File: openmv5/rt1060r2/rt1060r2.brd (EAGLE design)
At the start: 35.6 x 44.5 mm, 250 parts, among them CN1 S2B-PH-K-S(LF)(SN), IC1 LM66200DRLR, IC2 TCR2LF33,LM_CT, IC3 AP61300Z6-7, IC4 IS42S16160G-6BL, IC5 IS25LP128F-JKLE-TR, IC6 ATECC608B-MAHDA-T, IC7 MXC4005XC, IC8 KSZ8081RNDCA-TR, IC9 MIMXRT106FCVL5B, J1 USB4105-GF-A, J2 USD-1040310811, J3 DF12-36-DS, J4 DNP, J5 DNP, J6 DNP, J7 DNP, J8 3221-10-0300-00, J9 DNP, M1 9774030151R, M2 9774030151R, Q1 DMG2301L-7, Q2 2N7002KW_R1_00001, Q3 2N7002KW_R1_00001, Q4 2N7002KW_R1_00001, Q5 2N7002KW_R1_00001, U1 BQ24075RGTR, U2 LBEE5KL1DX-883, Y1 ECS-327MVATX-3-CN-TR3, Y2 XRCGB24M000F3M00R0, Y3 SC32S-7PF20PPM

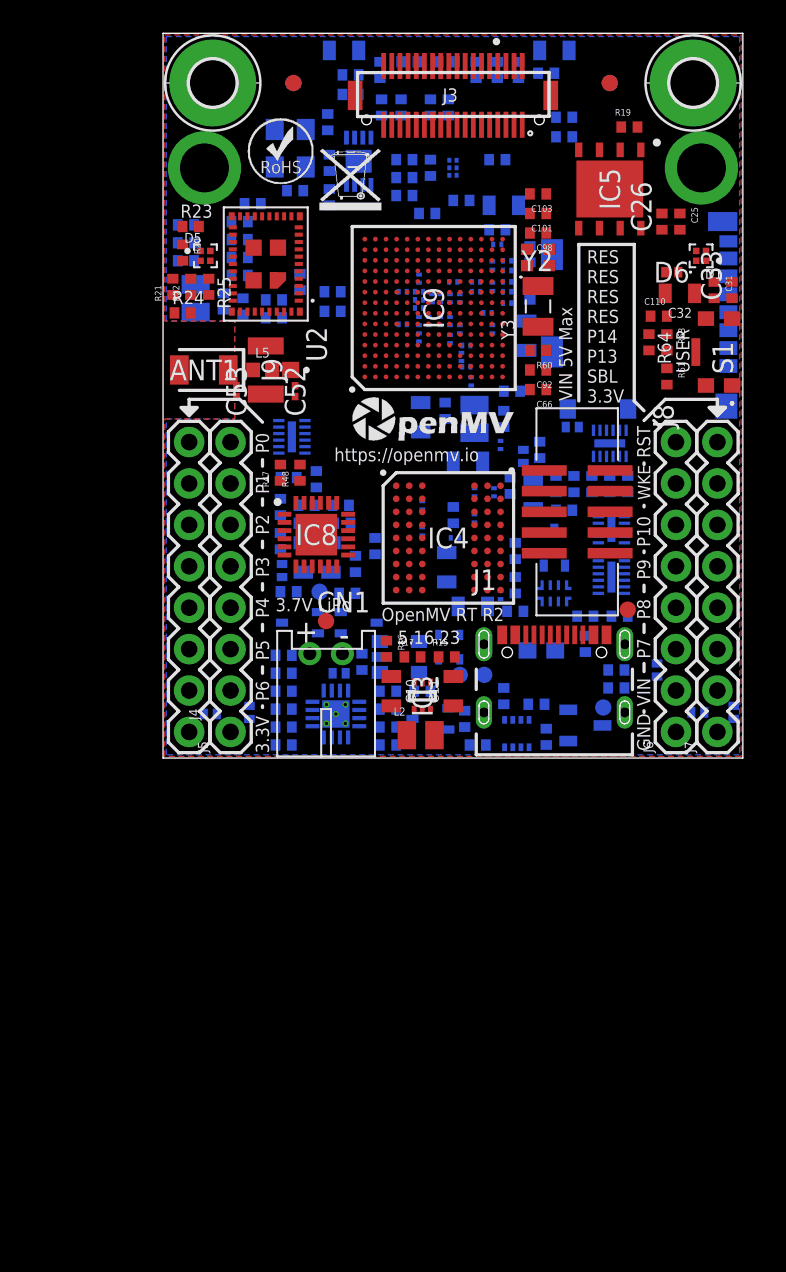
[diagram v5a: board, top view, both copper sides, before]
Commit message: Make the last two I/O pins more configurable
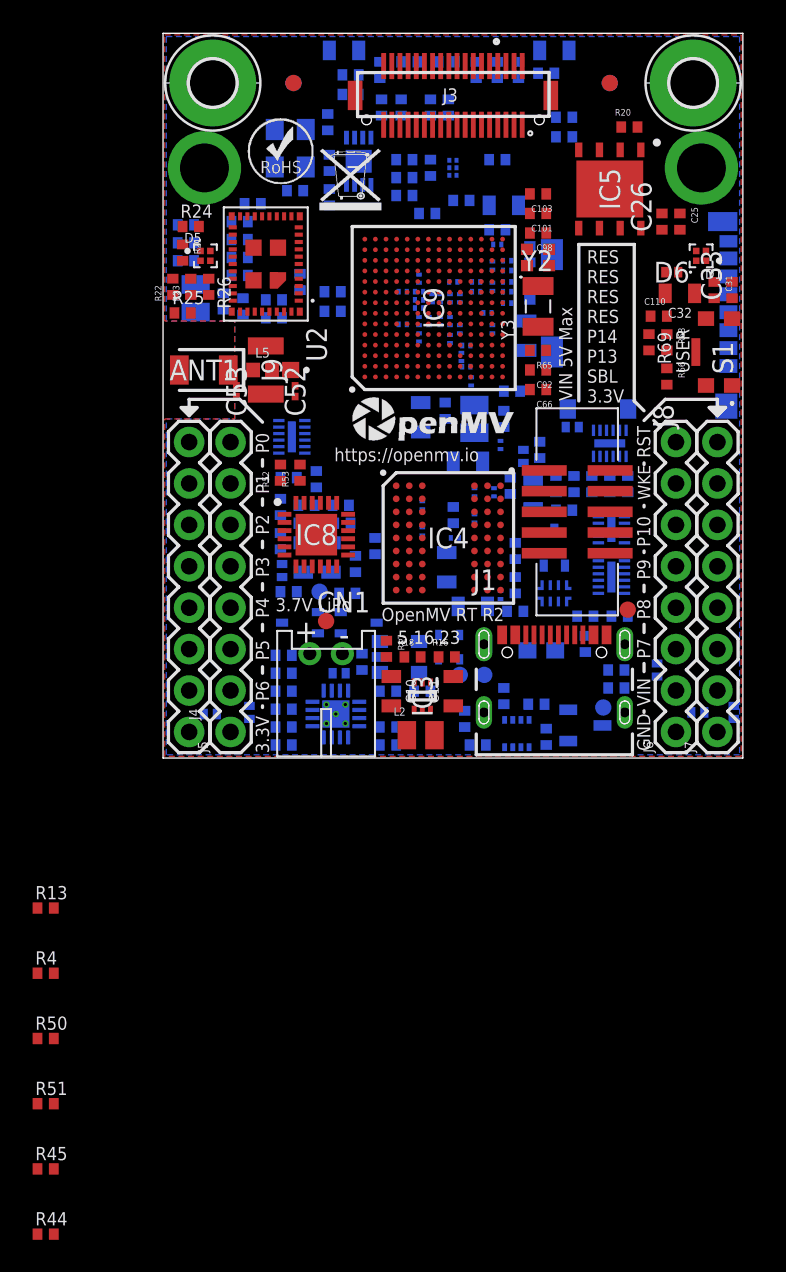
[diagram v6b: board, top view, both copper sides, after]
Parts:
- removed Q5: 2N7002KW_R1_00001, 2N7002KW_R1_00001:SOT65P210X110-3N
- added R65, R69: 100K, 0402:0402
- added R66, R68: 10K, 0402:0402
- added R67: 2.2M, 0402:0402
- R10: value 8.2K -> 46.4K
- R11: value 100K -> 8.2K
- R15: value 200K -> 100K
- R16: value 100K -> 200K
- R17: value 44.2K -> 100K
- R18: value 100K -> 44.2K
- R20, R4, R41: value 1K -> 100K
- R21, R43: value 10K -> 1K
- R22: value 5.1K -> 10K
- R23, R6: value 10K -> 5.1K
- R26: value 2.7K -> 10K
- R29: value 100K -> 2.7K
- R36, R52, R61, R63: value 10K -> 100K
- R38: value 4.7K -> 10K
- R40: value 100K -> 4.7K
- R44: value 10K -> 0
- R45: value DNP -> 0
- R46: value DNP -> 10K
- R47, R57, R58: value 100K -> 10K
- R48: value 220 -> DNP
- R49, R51: value 1K -> DNP
- R5: value 5.1K -> 1K
- R50: value 6.49K -> DNP
- R53: value 10K -> 220
- R54, R56: value 100K -> 1K
- R55: value 100K -> 6.49K
- R59: value 30K -> 100K
- R62: value 2.2M -> 100K
- R64: value 100K -> 30K
- R8: value 1.1K -> 10K
- R9: value 46.4K -> 1.1K
- moved R44 65.8 mm to (-7.20, -29.2), flipped to the top, turned to 0 degrees
- moved R45 46.2 mm to (-7.20, -25.2), flipped to the top, turned to 0 degrees
- moved R13 40.1 mm to (-7.20, -9.20), flipped to the top
- moved R51 38.2 mm to (-7.20, -21.2), flipped to the top, turned to 0 degrees
- moved R50 33.0 mm to (-7.20, -17.2), flipped to the top, turned to 0 degrees
- moved R4 30.0 mm to (-7.20, -13.2), flipped to the top
- moved R20 28.5 mm to (28.6, 38.7), turned to 0 degrees
- moved R46 27.4 mm to (16.2, 33.4), turned to 180 degrees
- moved R61 27.2 mm to (4.70, 30.7), flipped to the bottom, turned to 180 degrees
- moved R19 26.9 mm to (21.6, 12.7), flipped to the bottom, turned to 270 degrees
- moved R63 26.8 mm to (5.50, 34.0), flipped to the bottom, turned to 180 degrees
- moved R55 24.7 mm to (11.3, 10.1), turned to 180 degrees
- moved R60 22.9 mm to (1.40, 32.7), flipped to the bottom, turned to 0 degrees
- moved R35 22.8 mm to (28.5, 16.8), turned to 270 degrees
- moved R48 20.4 mm to (25.9, 7.00), flipped to the bottom
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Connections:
- removed net ON_BATTERY: IC9.P2, Q2.2, R12.1
- new net N$1: J6.3, R45.2
- new net N$2: J6.4, R44.2
- net BT_H_WAKE: now also R58.1; no longer R53.1
- net BT_REG_ON: now also R47.1; no longer R44.1
- net CHG: now also R13.1, R51.2, R6.1; no longer R5.1
- net DCDC_PSWITCH: now also R64.1; no longer R59.1
- net DCMI_D7: now also R46.1; no longer R43.1
- net DCMI_FSIN: now also R42.1; no longer R41.1
- net DCMI_PWDN: now also R38.1; no longer R37.1
- net DCMI_RST: now also R37.1; no longer R36.1
- net DCMI_SCL: now also R39.1; no longer R38.1
- net DCMI_SDA: now also R40.1; no longer R39.1
- net DCMI_SSEL: now also R36.1; no longer R35.1
- net EN: now also Q4.3, R17.1; no longer Q5.3, R16.1
- net ETH_INT: now also R54.1; no longer R49.1
- net ETH_LED: now also R53.1; no longer R48.1
- net ETH_MDIO: now also R56.1; no longer R51.1
- net ETH_RST: now also R52.1; no longer R47.1
- net FB: now also R16.1, R18.2; no longer R15.1, R17.2
- net GND: now also R11.2, R18.1, R37.2, R47.2, R55.2, R67.2; no longer R17.1, R36.2, R44.2, R50.2, R62.2, R7.2
- net ILIM: now also R9.1; no longer R8.1
- net INT_I2C_INT: now also R29.1; no longer R28.1
- net INT_I2C_SCL: now also R27.1; no longer R26.1
- net INT_I2C_SDA: now also R28.1; no longer R27.1
- net ISET: now also R11.1; no longer R10.1
- net JTAG_TDI: now also R50.1
- net JTAG_TDI_INT: now also R44.1, R48.1; no longer J6.4, R45.1
- net JTAG_TDI_INT_UNUSED: now also R48.2; no longer R45.2
- net JTAG_TRSTB: now also R51.1
- net JTAG_TRSTB_INT: now also R45.1, R49.1; no longer J6.3, R46.1
- net JTAG_TRSTB_INT_UNUSED: now also R49.2; no longer R46.2
- net LED_B: now also R21.1, R24.1; no longer R20.1, R23.1
- net LED_B_INT: now also R21.2; no longer R20.2
- net LED_CHG: now also R6.2; no longer R5.2
- net LED_G: now also R22.1, R25.1; no longer R21.1, R24.1
- net LED_G_INT: now also R22.2; no longer R21.2
- net LED_PGOOD: now also R7.2; no longer R6.2
- net LED_R: now also R23.1, R26.1; no longer R22.1, R25.1
- net LED_R_INT: now also R23.2; no longer R22.2
- net LED_ST: now also R5.2; no longer R4.2
- net MDI_LED: now also R53.2; no longer R48.2
- net ONOFF: now also Q3.2; no longer Q4.2
- net P10_PWM: now also R43.1; no longer R42.1
- net P11_WAKEUP: now also Q2.3, R14.1; no longer Q3.3, R13.1
- net P12_RST_N: now also R65.2; no longer R60.2
- net PGOOD: now also IC9.P2, R12.1, R7.1; no longer Q2.3, R11.1, R6.1
- net PMIC_ONOFF: now also Q3.3, R15.1; no longer Q4.3, R14.1
- net PMIC_ON_REQ: now also Q4.2; no longer Q5.2
- net PMIC_STBY_REQ: now also R69.1; no longer R64.1
- net PWM_FSIN: now also R41.1, R43.2; no longer R40.1, R41.2
- net P_FLASH_CE: now also R20.2; no longer R19.2
- net RAW: now also R15.2, R17.2; no longer D1.4, R11.2, R13.2, R16.2
- net REXT: now also R55.1; no longer R50.1
- net SBL: now also R46.2; no longer R43.2
- net SDRAM_CS: now also R19.2; no longer R18.2
- net SD_CD: now also R30.1; no longer R29.1
- net SD_CMD: now also R33.1; no longer R32.1
- net SD_DAT0: now also R32.1; no longer R31.1
- net SD_DAT1: now also R31.1; no longer R30.1
- net SD_DAT2: now also R35.1; no longer R34.1
- net SD_DAT3: now also R34.1; no longer R33.1
- net ST: now also R5.1, R50.2
- net SWITCH: now also R66.1, R68.2; no longer R61.1, R63.2
- net SWITCH_OUT: now also R68.1, R69.2; no longer R63.1, R64.2
- net TMR: now also R10.1; no longer R9.1
- net TS: now also R8.1; no longer R7.1
- net VCC: now also D1.4, R13.2, R16.2, R20.1, R36.2, R4.2, R41.2, R60.2, R62.2, R63.2, R64.2, R65.1, R66.2; no longer Q2.1, R15.2, R18.1, R23.2, R37.2, R47.2, R49.2, R51.2, R53.2, R55.2, R60.1
- net VDD_SNVS: now also Q2.1; no longer Q5.1
- net WAKEUP: now also Q2.2; no longer Q3.2
- net WIFI_CMD: now also R63.1; no longer R58.1
- net WIFI_D0: now also R62.1; no longer R57.1
- net WIFI_D1: now also R61.1; no longer R56.1
- net WIFI_D2: now also R60.1; no longer R55.1
- net WIFI_D3: now also R59.1; no longer R54.1
- net WL_H_WAKE: now also R57.1; no longer R52.1
- net XTALI: now also R67.1; no longer R62.1

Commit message: Cleanup
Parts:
- moved R44 53.6 mm to (29.6, 9.80), flipped to the bottom, turned to 270 degrees
- moved R45 49.3 mm to (29.6, 7.60), flipped to the bottom, turned to 270 degrees
- moved R51 45.1 mm to (13.2, 19.0), flipped to the bottom, turned to 90 degrees
- moved R50 42.2 mm to (14.4, 19.0), flipped to the bottom, turned to 90 degrees
- moved R4 40.6 mm to (14.4, 21.2), flipped to the bottom, turned to 90 degrees
- moved R13 36.6 mm to (13.2, 21.2), flipped to the bottom, turned to 90 degrees
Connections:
- net N$1 renamed P13
- net N$2 renamed P14
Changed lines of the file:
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@@
 <attribute name="VALUE" x="18.905" y="40.535" size="0.8128" layer="28" ratio="10" rot="MR270"/>
 </element>
-<element name="R13" library="0402" package="0402" value="100K" x="-7.2" y="-9.2" smashed="yes">
-<attribute name="MPN" value="AC0402FR-07100KL" x="-7.2" y="-9.2" size="1.778" layer="27" display="off"/>
-<attribute name="NAME" x="-7.835" y="-8.665" size="0.8128" layer="25" ratio="10"/>
-<attribute name="VALUE" x="-7.835" y="-10.605" size="0.8128" layer="27" ratio="10"/>
+<element name="R13" library="0402" package="0402" value="100K" x="13.2" y="21.2" smashed="yes" rot="MR90">
+<attribute name="MPN" value="AC0402FR-07100KL" x="13.2" y="21.2" size="1.778" layer="28" rot="MR90" display="off"/>
+<attribute name="NAME" x="13.735" y="20.565" size="0.8128" layer="26" ratio="10" rot="MR90"/>
+<attribute name="VALUE" x="11.795" y="20.565" size="0.8128" layer="28" ratio="10" rot="MR90"/>
 </element>
-<element name="R4" library="0402" package="0402" value="100K" x="-7.2" y="-13.2" smashed="yes">
-<attribute name="MPN" value="AC0402FR-07100KL" x="-7.2" y="-13.2" size="1.778" layer="27" display="off"/>
-<attribute name="NAME" x="-7.835" y="-12.665" size="0.8128" layer="25" ratio="10"/>
-<attribute name="VALUE" x="-7.835" y="-14.605" size="0.8128" layer="27" ratio="10"/>
+<element name="R4" library="0402" package="0402" value="100K" x="14.4" y="21.2" smashed="yes" rot="MR90">
+<attribute name="MPN" value="AC0402FR-07100KL" x="14.4" y="21.2" size="1.778" layer="28" rot="MR90" display="off"/>
+<attribute name="NAME" x="14.935" y="20.565" size="0.8128" layer="26" ratio="10" rot="MR90"/>
+<attribute name="VALUE" x="12.995" y="20.565" size="0.8128" layer="28" ratio="10" rot="MR90"/>
 </element>
-<element name="R50" library="0402" package="0402" value="DNP" x="-7.2" y="-17.2" smashed="yes">
-<attribute name="MPN" value="DNP" x="-7.2" y="-17.2" size="1.778" layer="27" display="off"/>
-<attribute name="NAME" x="-7.835" y="-16.665" size="0.8128" layer="25" ratio="10"/>
-<attribute name="VALUE" x="-7.835" y="-18.605" size="0.8128" layer="27" ratio="10"/>
+<element name="R50" library="0402" package="0402" value="DNP" x="14.4" y="19" smashed="yes" rot="MR90">
+<attribute name="MPN" value="DNP" x="14.4" y="19" size="1.778" layer="28" rot="MR90" display="off"/>
+<attribute name="NAME" x="14.935" y="18.365" size="0.8128" layer="26" ratio="10" rot="MR90"/>
+<attribute name="VALUE" x="12.995" y="18.365" size="0.8128" layer="28" ratio="10" rot="MR90"/>
 </element>
-<element name="R51" library="0402" package="0402" value="DNP" x="-7.2" y="-21.2" smashed="yes">
-<attribute name="MPN" value="DNP" x="-7.2" y="-21.2" size="1.778" layer="27" display="off"/>
-<attribute name="NAME" x="-7.835" y="-20.665" size="0.8128" layer="25" ratio="10"/>
-<attribute name="VALUE" x="-7.835" y="-22.605" size="0.8128" layer="27" ratio="10"/>
+<element name="R51" library="0402" package="0402" value="DNP" x="13.2" y="19" smashed="yes" rot="MR90">
+<attribute name="MPN" value="DNP" x="13.2" y="19" size="1.778" layer="28" rot="MR90" display="off"/>
+<attribute name="NAME" x="13.735" y="18.365" size="0.8128" layer="26" ratio="10" rot="MR90"/>
+<attribute name="VALUE" x="11.795" y="18.365" size="0.8128" layer="28" ratio="10" rot="MR90"/>
 </element>
-<element name="R45" library="0402" package="0402" value="0" x="-7.2" y="-25.2" smashed="yes">
-<attribute name="MPN" value="RC0402JR-070RL" x="-7.2" y="-25.2" size="1.778" layer="27" display="off"/>
-<attribute name="NAME" x="-7.835" y="-24.665" size="0.8128" layer="25" ratio="10"/>
-<attribute name="VALUE" x="-7.835" y="-26.605" size="0.8128" layer="27" ratio="10"/>
+<element name="R45" library="0402" package="0402" value="0" x="29.6" y="7.6" smashed="yes" rot="MR270">
+<attribute name="MPN" value="RC0402JR-070RL" x="29.6" y="7.6" size="1.778" layer="28" rot="MR270" display="off"/>
+<attribute name="NAME" x="29.065" y="8.235" size="0.8128" layer="26" ratio="10" rot="MR270"/>
+<attribute name="VALUE" x="31.005" y="8.235" size="0.8128" layer="28" ratio="10" rot="MR270"/>
 </element>
-<element name="R44" library="0402" package="0402" value="0" x="-7.2" y="-29.2" smashed="yes">
-<attribute name="MPN" value="RC0402JR-070RL" x="-7.2" y="-29.2" size="1.778" layer="27" display="off"/>
-<attribute name="NAME" x="-7.835" y="-28.665" size="0.8128" layer="25" ratio="10"/>
-<attribute name="VALUE" x="-7.835" y="-30.605" size="0.8128" layer="27" ratio="10"/>
+<element name="R44" library="0402" package="0402" value="0" x="29.6" y="9.8" smashed="yes" rot="MR270">
+<attribute name="MPN" value="RC0402JR-070RL" x="29.6" y="9.8" size="1.778" layer="28" rot="MR270" display="off"/>
+<attribute name="NAME" x="29.065" y="10.435" size="0.8128" layer="26" ratio="10" rot="MR270"/>
+<attribute name="VALUE" x="31.005" y="10.435" size="0.8128" layer="28" ratio="10" rot="MR270"/>
 </element>
 </elements>
@@
 <wire x1="17.3" y1="21.8" x2="18.875" y2="23.375" width="0" layer="19" extent="1-16"/>
 <wire x1="15.8" y1="21.8" x2="17.3" y2="21.8" width="0" layer="19" extent="16-16"/>
+<wire x1="14.4" y1="21.7" x2="15.8" y2="21.8" width="0" layer="19" extent="16-16"/>
+<wire x1="13.2" y1="21.7" x2="14.4" y2="21.7" width="0" layer="19" extent="16-16"/>
 <wire x1="21.9" y1="22.5" x2="18.9" y2="23.35" width="0" layer="19" extent="16-16"/>
 <wire x1="22.5" y1="22.6" x2="21.9" y2="22.5" width="0" layer="19" extent="1-16"/>
@@
 <wire x1="31.46" y1="1.6" x2="21.6" y2="10.1" width="0" layer="19" extent="16-16"/>
 <wire x1="32.4" y1="2.8" x2="31.46" y2="1.6" width="0" layer="19" extent="16-16"/>
-<wire x1="-6.7" y1="-9.2" x2="1.6" y2="1.6" width="0" layer="19" extent="1-1"/>
-<wire x1="-6.7" y1="-13.2" x2="-6.7" y2="-9.2" width="0" layer="19" extent="1-1"/>
 </signal>
 <signal name="DCMI_D0" class="5">
@@
 <contactref element="R13" pad="1"/>
 <contactref element="R51" pad="2"/>
-<wire x1="-7.7" y1="-9.2" x2="-6.7" y2="-21.2" width="0" layer="19" extent="1-1"/>
-<wire x1="11.35" y1="1.265" x2="-7.7" y2="-9.2" width="0" layer="19" extent="1-16"/>
+<wire x1="11.35" y1="1.265" x2="13.2" y2="20.7" width="0" layer="19" extent="16-16"/>
 <wire x1="13.3" y1="0.8" x2="11.35" y2="1.265" width="0" layer="19" extent="16-16"/>
+<wire x1="13.2" y1="19.5" x2="11.35" y2="1.265" width="0" layer="19" extent="1-16"/>
 </signal>
 <signal name="CC1">
@@
 <contactref element="R4" pad="1"/>
 <contactref element="R50" pad="2"/>
-<wire x1="19.8" y1="0.8" x2="20.95" y2="0.662" width="0" layer="19" extent="16-16"/>
-<wire x1="-7.7" y1="-13.2" x2="19.8" y2="0.8" width="0" layer="19" extent="1-16"/>
-<wire x1="-6.7" y1="-17.2" x2="-7.7" y2="-13.2" width="0" layer="19" extent="1-1"/>
+<wire x1="14.4" y1="19.5" x2="14.4" y2="20.7" width="0" layer="19" extent="16-16"/>
+<wire x1="19.8" y1="0.8" x2="14.4" y2="19.5" width="0" layer="19" extent="16-16"/>
+<wire x1="20.95" y1="0.662" x2="19.8" y2="0.8" width="0" layer="19" extent="16-16"/>
 </signal>
 <signal name="LED_ST">
@@
 <contactref element="R44" pad="1"/>
 <wire x1="25.9" y1="6.5" x2="28.3" y2="10.9" width="0" layer="19" extent="16-16"/>
-<wire x1="-7.7" y1="-29.2" x2="25.9" y2="6.5" width="0" layer="19" extent="1-16"/>
+<wire x1="29.6" y1="10.3" x2="25.9" y2="6.5" width="0" layer="19" extent="1-16"/>
 </signal>
 <signal name="P12_RST_N_EXT">
@@
 <contactref element="R50" pad="1"/>
 <wire x1="26.7" y1="10.9" x2="15.625" y2="31.825" width="0" layer="19" extent="1-16"/>
-<wire x1="-7.7" y1="-17.2" x2="26.7" y2="10.9" width="0" layer="19" extent="1-16"/>
+<wire x1="14.4" y1="18.5" x2="26.7" y2="10.9" width="0" layer="19" extent="1-16"/>
 </signal>
 <signal name="JTAG_TRSTB" class="4">
@@
 <contactref element="R51" pad="1"/>
 <wire x1="26.7" y1="10.1" x2="16.275" y2="29.225" width="0" layer="19" extent="1-16"/>
-<wire x1="-7.7" y1="-21.2" x2="26.7" y2="10.1" width="0" layer="19" extent="1-16"/>
+<wire x1="13.2" y1="18.5" x2="26.7" y2="10.1" width="0" layer="19" extent="1-16"/>
 </signal>
 <signal name="P12_RST_N">
@@
 <contactref element="R45" pad="1"/>
 <wire x1="28.5" y1="8.7" x2="28.3" y2="10.1" width="0" layer="19" extent="16-16"/>
-<wire x1="-7.7" y1="-25.2" x2="28.5" y2="8.7" width="0" layer="19" extent="1-16"/>
+<wire x1="29.6" y1="8.1" x2="28.5" y2="8.7" width="0" layer="19" extent="1-16"/>
 </signal>
 <signal name="DCMI_SCL" class="13">
@@
 <wire x1="17.5" y1="39.4" x2="16.4" y2="39.4" width="0" layer="19" extent="1-1"/>
 </signal>
-<signal name="N$1" class="4">
+<signal name="P13" class="4">
 <contactref element="J6" pad="3"/>
 <contactref element="R45" pad="2"/>
-<wire x1="-6.7" y1="-25.2" x2="31.46" y2="6.68" width="0" layer="19" extent="1-1"/>
-</signal>
-<signal name="N$2" class="4">
+<wire x1="29.6" y1="7.1" x2="31.46" y2="6.68" width="0" layer="19" extent="16-16"/>
+</signal>
+<signal name="P14" class="4">
 <contactref element="J6" pad="4"/>
 <contactref element="R44" pad="2"/>
-<wire x1="-6.7" y1="-29.2" x2="31.46" y2="9.22" width="0" layer="19" extent="1-1"/>
+<wire x1="29.6" y1="9.3" x2="31.46" y2="9.22" width="0" layer="19" extent="16-16"/>
 </signal>
 </signals>
